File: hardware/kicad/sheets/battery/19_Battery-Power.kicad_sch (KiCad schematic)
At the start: 40 parts, among them Q19 IPT012N08N5(TOKMAS), Q20 IPT012N08N5(TOKMAS), Q22 ZXMP10A17GTA, Q23 BSS84AK,215, Q24 BSS123NH6327

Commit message: various improvements
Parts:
- renumbered C113 to C114, C114 to C115, C119 to C118, C120 to C119, D31 to D34, D36 to D35, D32 to D36, D33 to D38, D34 to D39, D38 to D40, D39 to D41, D40 to D42, Q19 to Q20, Q20 to Q21, R163 to R164, R164 to R165, R165 to R166, R166 to R167, R175 to R169, R176 to R170, R180 to R174, R167 to R175, R169 to R176, R170 to R177, R179 to R178, R181 to R179, R182 to R180, R183 to R181

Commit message: various improvements
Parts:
- renumbered C114 to C120, C115 to C121, C116 to C122, C117 to C123, C118 to C124, C119 to C125, D34 to D35, D35 to D36, D36 to D37, D37 to D38, D38 to D39, D39 to D40, D40 to D41, D41 to D42, D42 to D43, NT24 to NT25, NT25 to NT26, Q20 to Q21, Q21 to Q22, Q22 to Q23, Q23 to Q24, Q24 to Q25, R164 to R175, R165 to R176, R166 to R177, R167 to R178, R168 to R179, R169 to R180, R170 to R181, R171 to R182, R172 to R183, R173 to R184, R174 to R185, R175 to R186, R176 to R187, R177 to R188, R178 to R189, R179 to R190, R180 to R191, R181 to R192

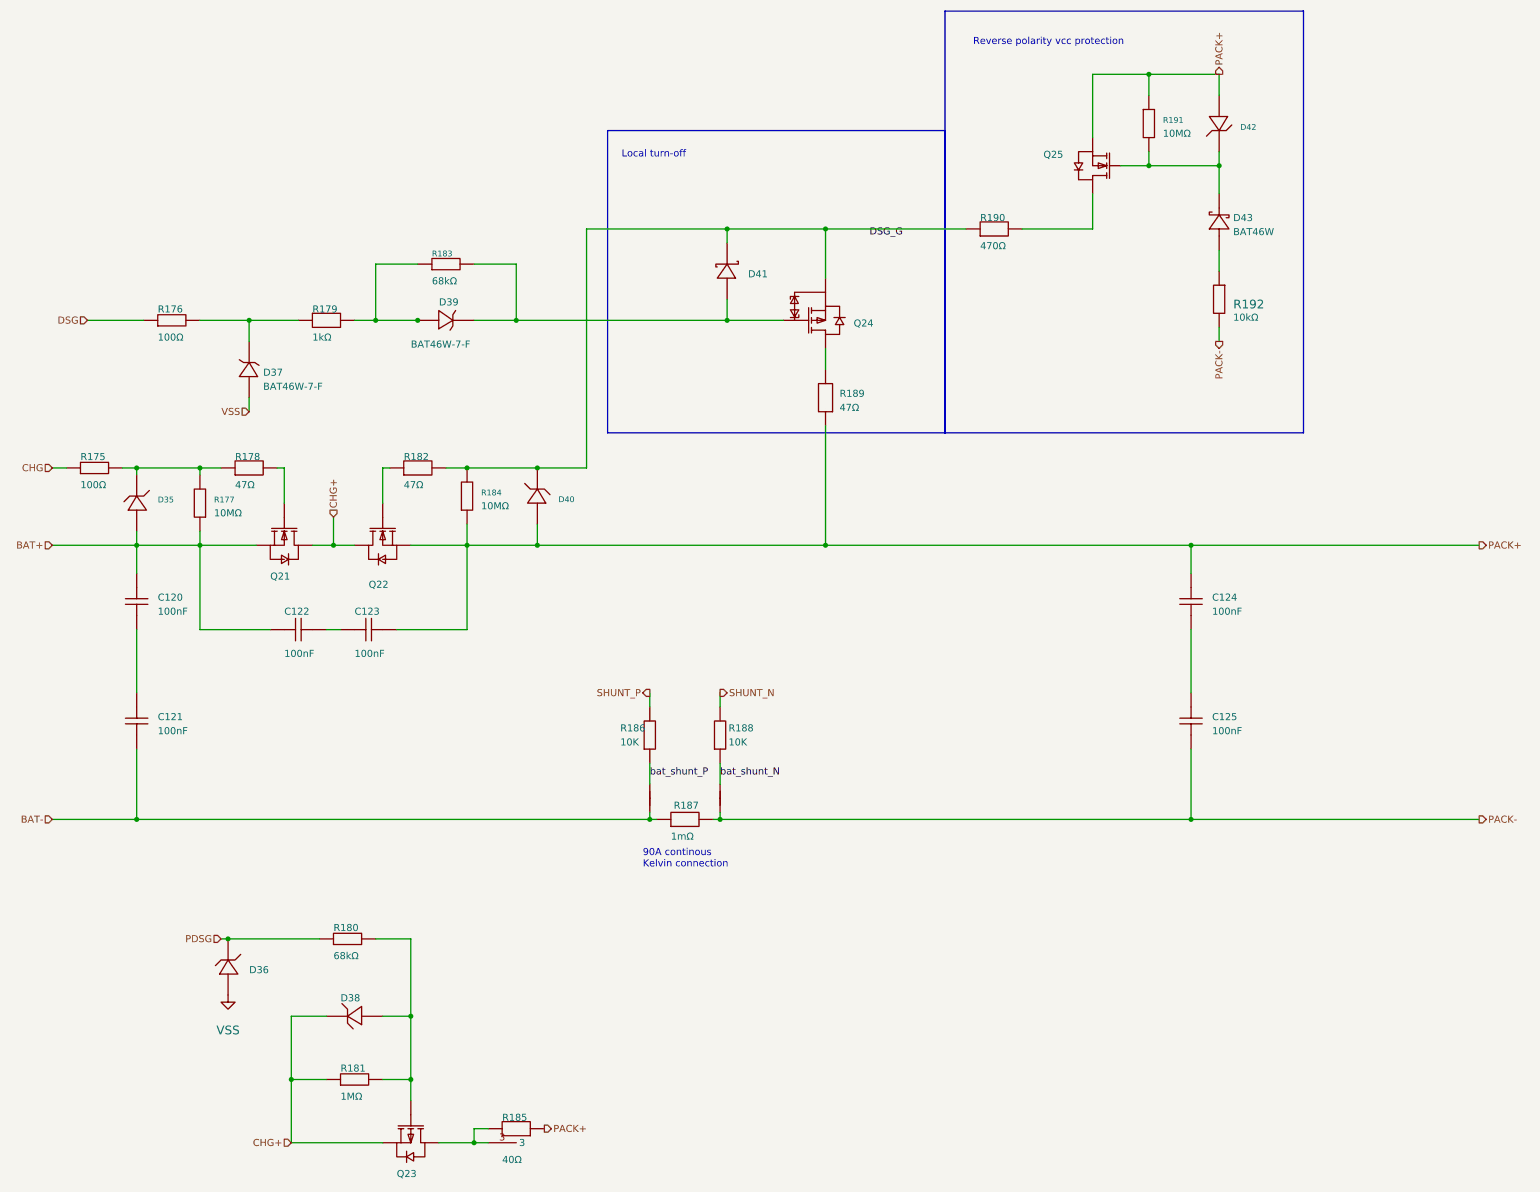
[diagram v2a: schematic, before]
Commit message: current sensing on the servos and cleaning up empty sheets
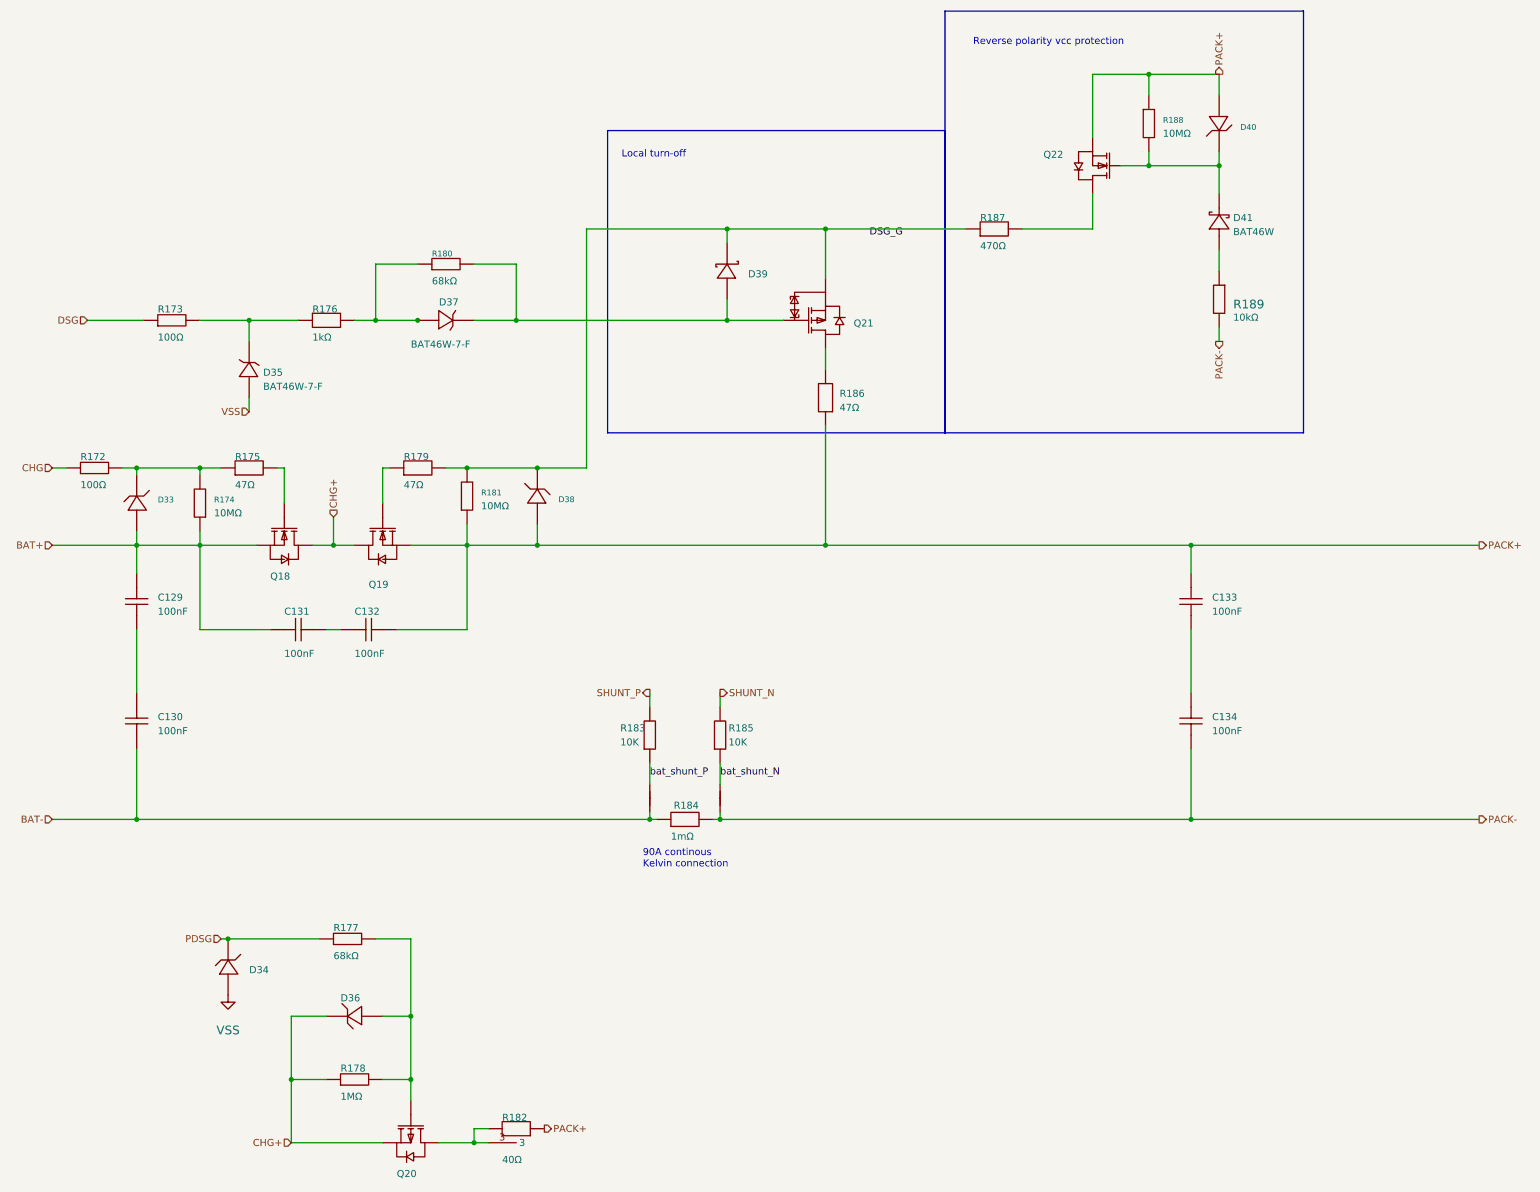
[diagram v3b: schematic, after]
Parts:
- renumbered C120 to C129, C121 to C130, C122 to C131, C123 to C132, C124 to C133, C125 to C134, D35 to D33, D36 to D34, D37 to D35, D38 to D36, D39 to D37, D40 to D38, D41 to D39, D42 to D40, D43 to D41, NT25 to NT27, NT26 to NT28, Q21 to Q18, Q22 to Q19, Q23 to Q20, Q24 to Q21, Q25 to Q22, R175 to R172, R176 to R173, R177 to R174, R178 to R175, R179 to R176, R180 to R177, R181 to R178, R182 to R179, R183 to R180, R184 to R181, R185 to R182, R186 to R183, R187 to R184, R188 to R185, R189 to R186, R190 to R187, R191 to R188, R192 to R189

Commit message: new references
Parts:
- renumbered C129 to C119, C130 to C120, C131 to C121, C132 to C122, C133 to C125, C134 to C126, D33 to D29, D34 to D30, D35 to D31, D36 to D32, D37 to D33, D38 to D34, D39 to D35, D40 to D36, D41 to D37, NT27 to NT24, NT28 to NT25, Q18 to Q13, Q19 to Q14, Q20 to Q15, Q21 to Q16, Q22 to Q17, R172 to R151, R173 to R153, R174 to R154, R175 to R156, R176 to R161, R177 to R162, R178 to R163, R179 to R164, R180 to R165, R181 to R166, R182 to R167, R183 to R169, R184 to R170, R185 to R172, R186 to R173, R187 to R174, R188 to R175, R189 to R176

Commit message: pre robot updating references
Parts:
- renumbered C119 to C117, C120 to C118, C121 to C119, C122 to C120, C125 to C123, C126 to C124, NT24 to NT27, NT25 to NT28, R151 to R158, R153 to R160, R154 to R161, R156 to R163, R161 to R168, R162 to R169, R163 to R170, R164 to R171, R165 to R172, R166 to R173, R167 to R174, R169 to R176, R170 to R177, R172 to R179, R173 to R180, R174 to R181, R175 to R182, R176 to R183

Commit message: various imprvements
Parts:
- renumbered C117 to C126, C118 to C127, C119 to C128, C120 to C129, C123 to C131, C124 to C132, D35 to D36, D36 to D37, D37 to D38, NT27 to NT29, NT28 to NT30, Q13 to Q14, Q14 to Q15, Q15 to Q16, Q16 to Q17, Q17 to Q18, R158 to R198, R160 to R202, R161 to R203, R163 to R205, R168 to R206, R169 to R207, R170 to R208, R171 to R209, R172 to R210, R173 to R211, R174 to R212, R176 to R213, R177 to R214, R179 to R215, R180 to R216, R181 to R217, R182 to R218, R183 to R219

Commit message: updated some footprints, fixed board
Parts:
- renumbered C126 to C122, C127 to C123, C128 to C124, C129 to C125, C131 to C128, C132 to C129, D36 to D35, D37 to D36, D38 to D37, Q14 to Q13, Q15 to Q14, Q16 to Q15, Q17 to Q16, Q18 to Q17, R198 to R197, R202 to R198, R203 to R199, R205 to R200, R206 to R201, R207 to R202, R208 to R203, R209 to R204, R210 to R205, R211 to R206, R212 to R207, R213 to R208, R214 to R209, R215 to R210, R216 to R211, R217 to R212, R218 to R213, R219 to R214

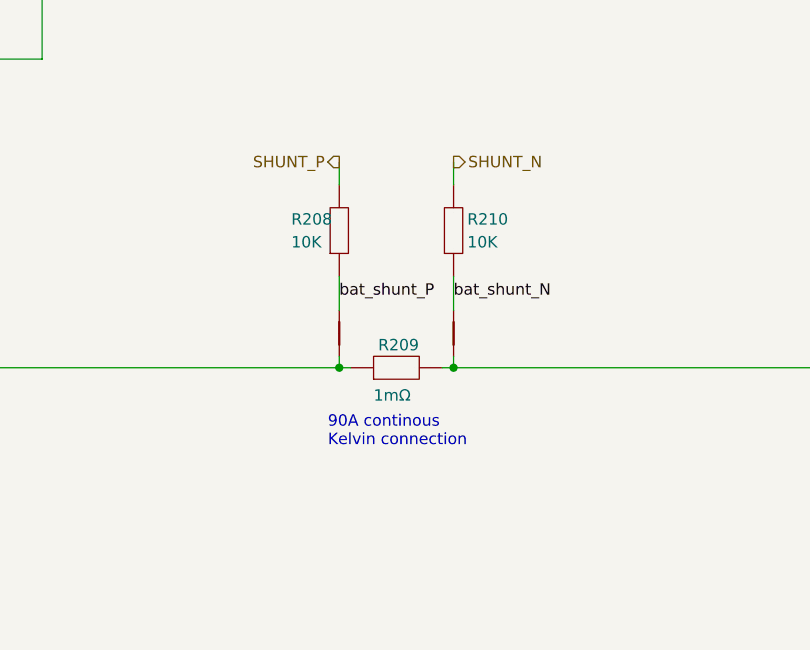
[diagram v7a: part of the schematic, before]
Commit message: various changes
removed mistakenly placed 100k resistors bms
changed to 25ppm/C sense resistor as recommended by datasheet bms
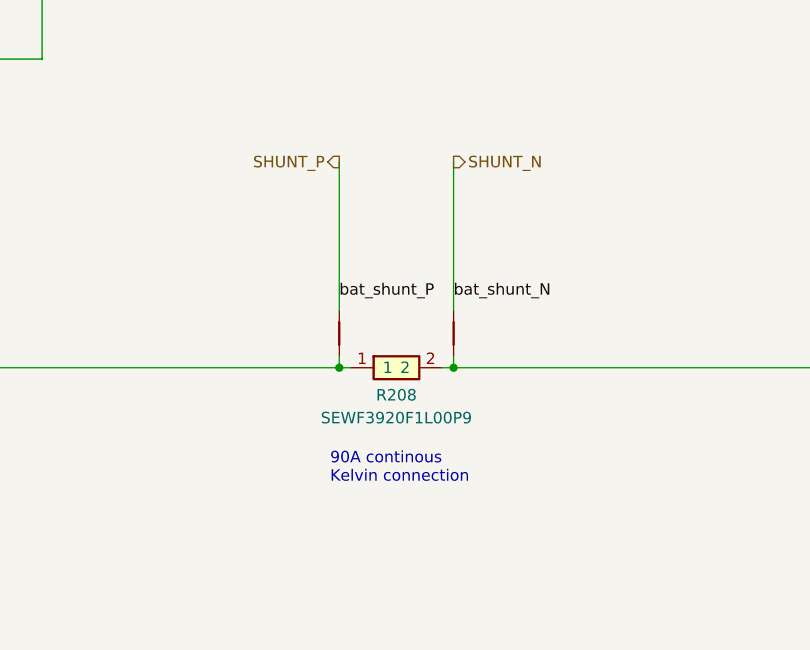
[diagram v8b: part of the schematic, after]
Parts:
- removed R208, R210: 10K, Resistor_SMD:R_0402_1005Metric, symbol 5v rail sm-easyedapro:Res
- removed R209: 1mΩ, 5v rail sm-easyedapro:R3920, symbol 5v rail sm-easyedapro:PEWM3920F1L00K9
- added R208: SEWF3920F1L00P9, JLCImport:SEWF3920F1L00P9, symbol JLCImport:SEWF3920F1L00P9
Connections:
- net bat_shunt_N is gone; now on net SHUNT_N: NT30.1
- net bat_shunt_P is gone; now on net SHUNT_P: NT29.1
- net BAT-: now also R208.1
- net PACK-: now also R208.2
